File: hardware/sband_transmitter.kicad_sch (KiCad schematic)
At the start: 0 parts

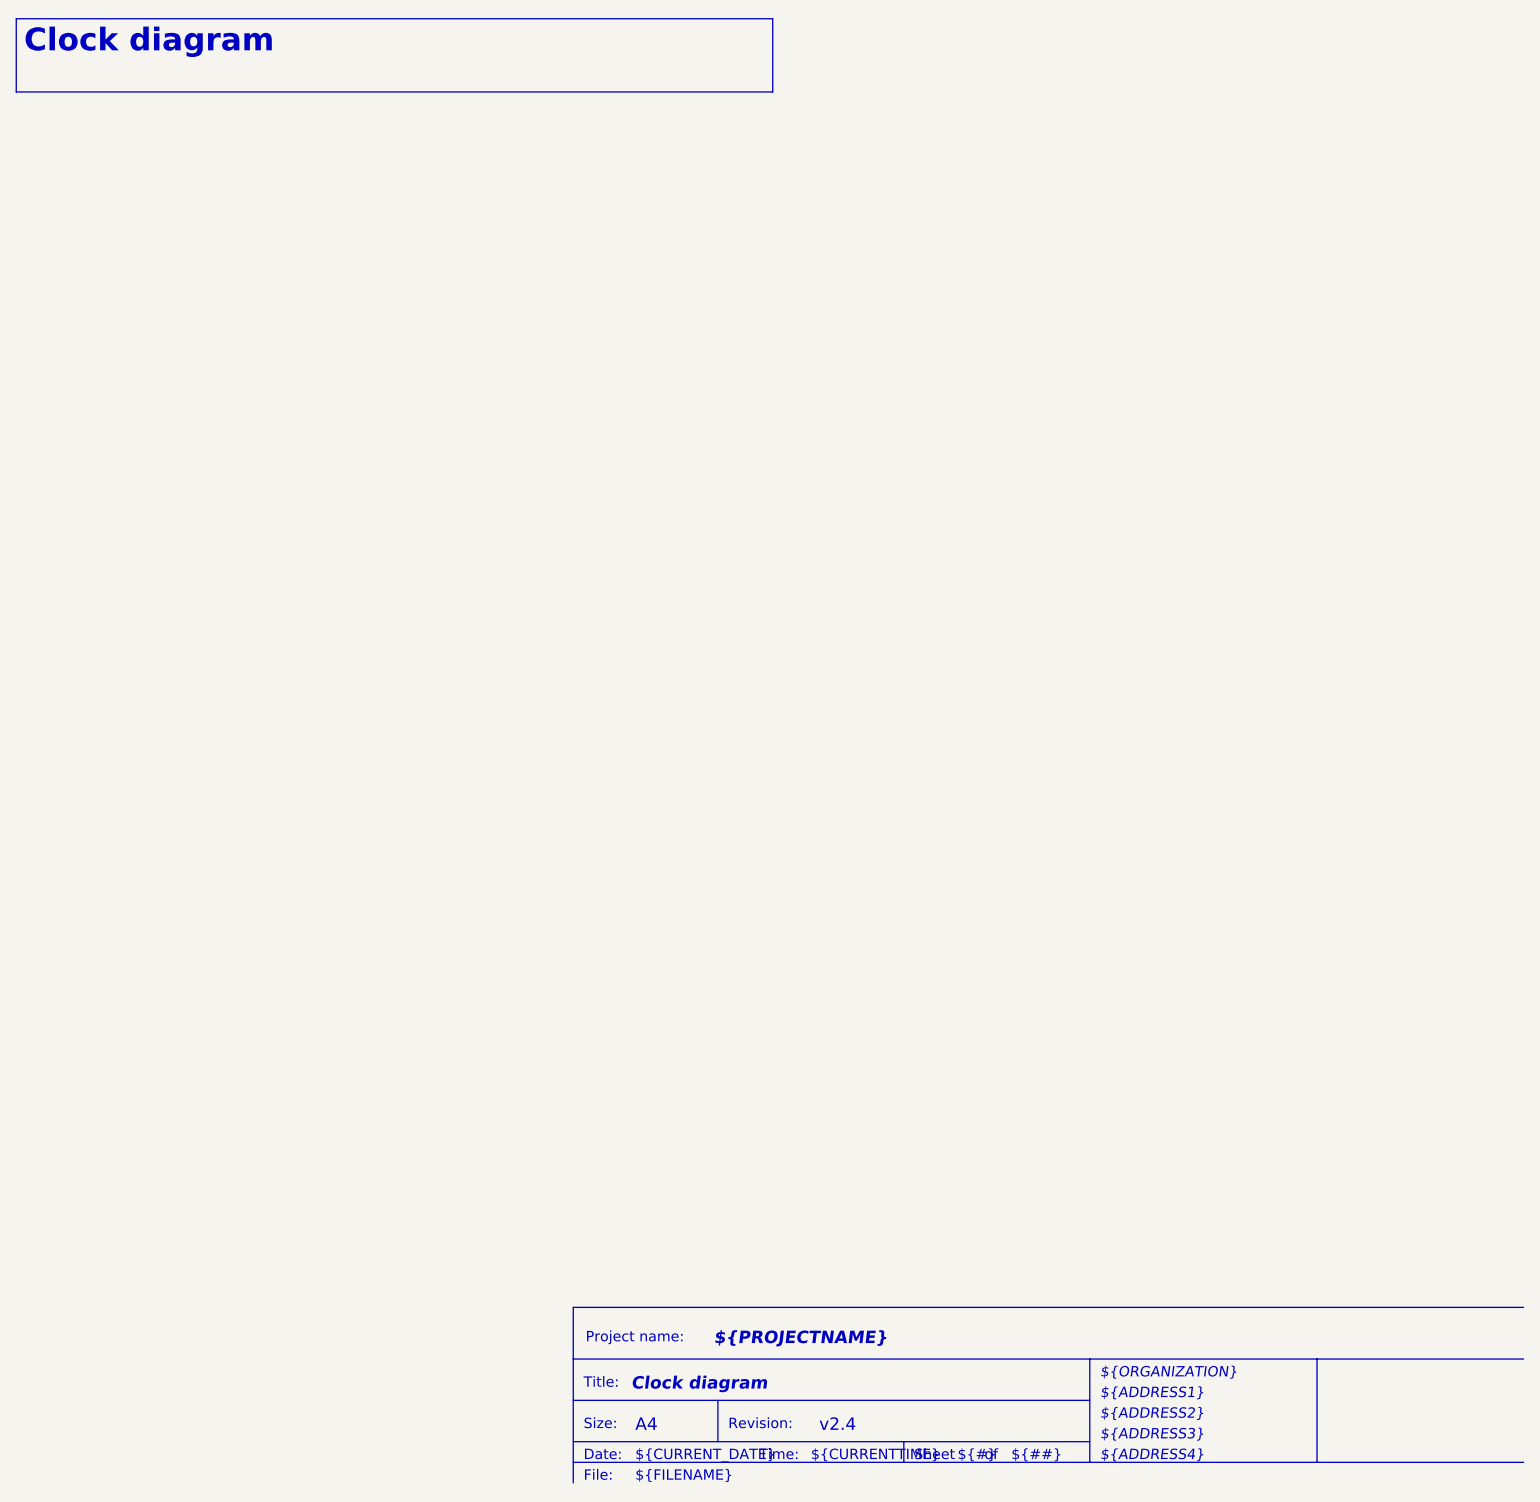
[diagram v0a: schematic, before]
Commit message: Updated sheet names, added s-band initial block diagram
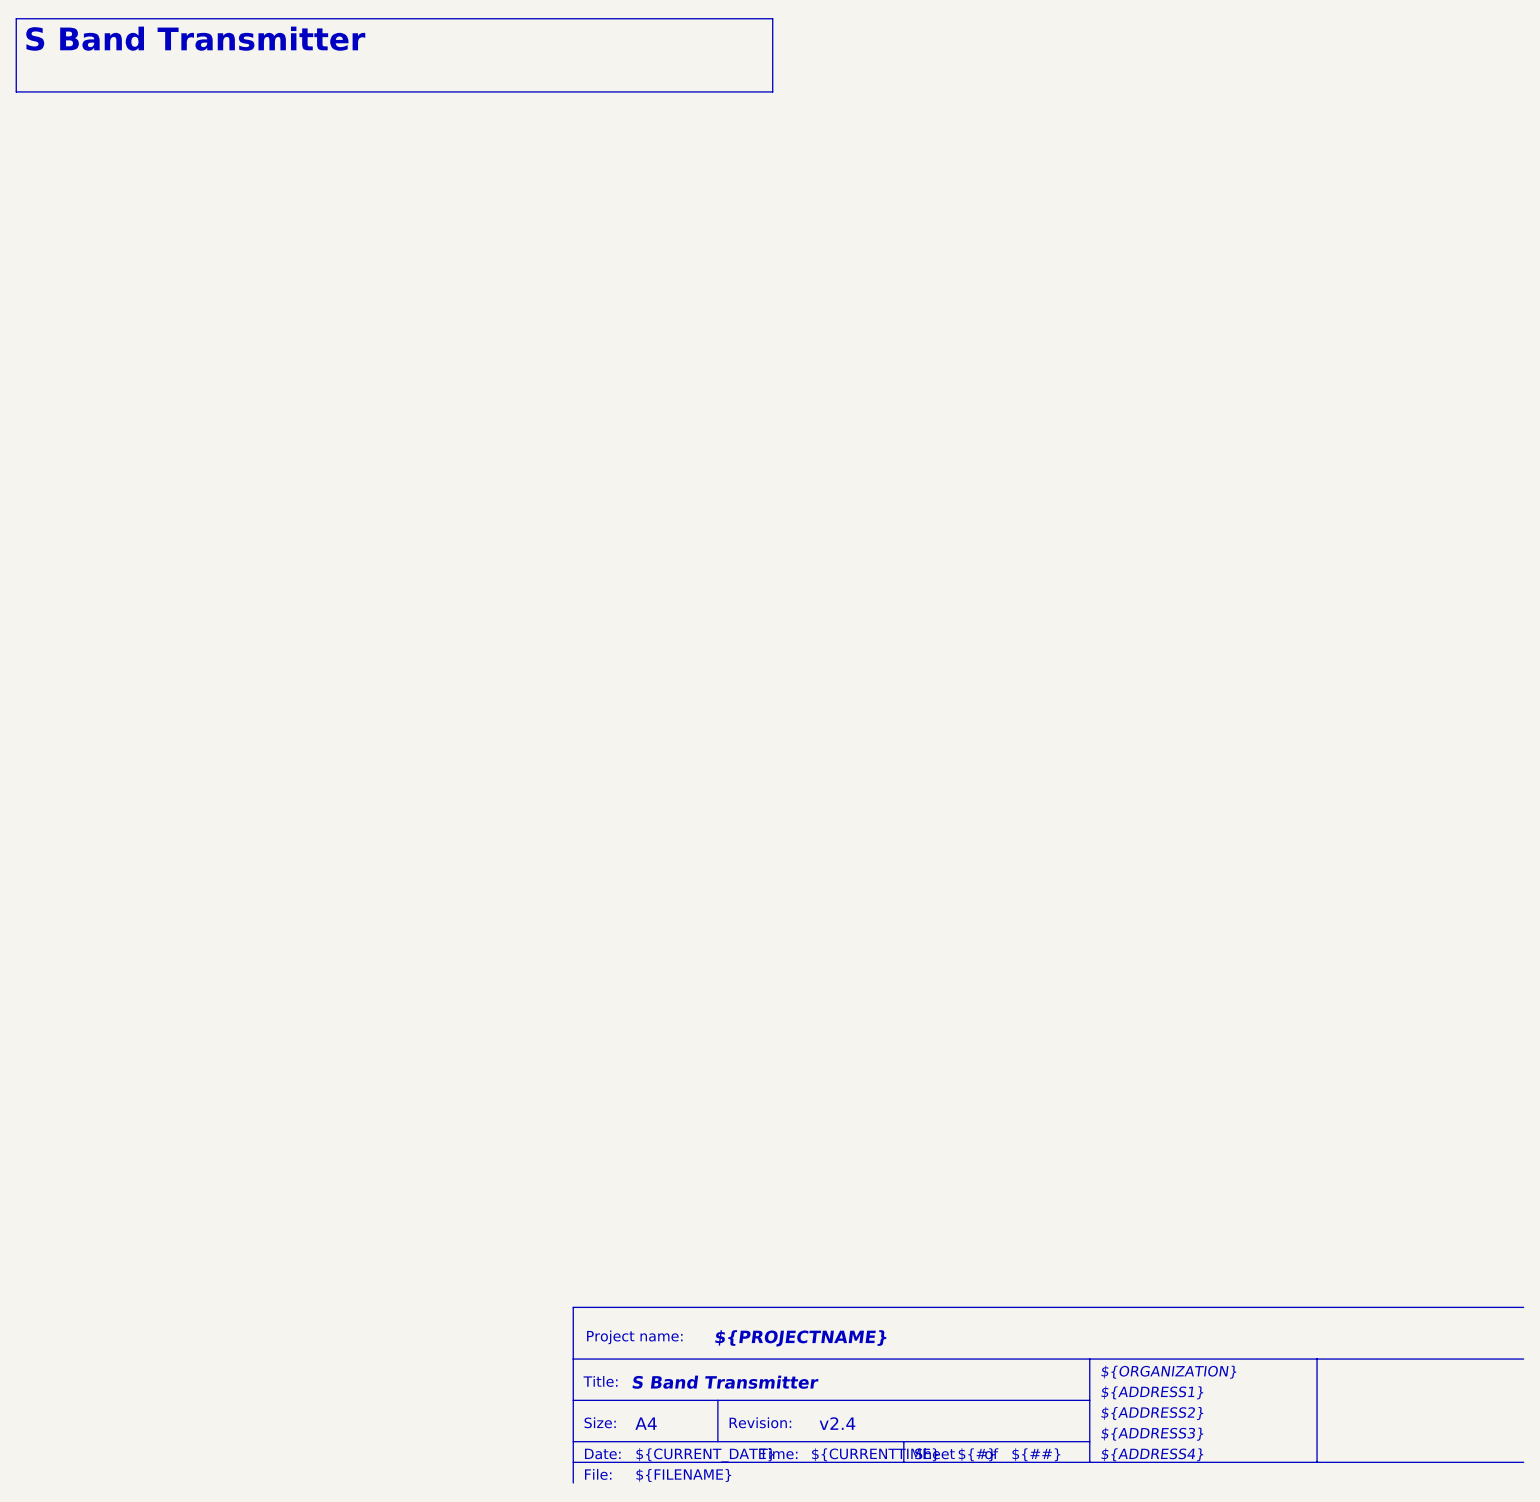
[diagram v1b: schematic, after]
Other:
- title: Clock diagram -> S Band Transmitter
